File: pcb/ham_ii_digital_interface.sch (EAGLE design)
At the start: 21 parts, among them IC1 LM358N, T1 Left Driver, T2 Brake Driver, T3 Right Driver

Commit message: Changed value of C1 and changed C1 to an electrolytic capacitor.
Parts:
- C1: value 220p -> 1u; device resistor:C-US050-025X075 -> resistor:CPOL-USE2-5
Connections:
- net GND: now also C1.-; no longer C1.2
- net N$1: now also C1.+; no longer C1.1
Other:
- moved on the sheet: JP1, JP2
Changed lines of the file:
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@@
 <part name="D3" library="diode" deviceset="1N4148" device="DO35-7"/>
 <part name="JP2" library="pinhead" deviceset="PINHD-1X6" device="" value="Test"/>
-<part name="C1" library="resistor" deviceset="C-US" device="050-025X075" value="220p"/>
+<part name="C1" library="resistor" deviceset="CPOL-US" device="E2-5" value="1u"/>
 </parts>
 <sheets>
@@
 </plain>
 <instances>
-<instance part="JP1" gate="G$1" x="15.24" y="7.62"/>
-<instance part="JP2" gate="A" x="15.24" y="-12.7"/>
+<instance part="JP1" gate="G$1" x="17.78" y="7.62"/>
+<instance part="JP2" gate="A" x="17.78" y="-12.7"/>
 </instances>
 <busses>
@@
 <net name="LEFT_CONTROL_SIGNAL" class="0">
 <segment>
-<wire x1="12.7" y1="-5.08" x2="-22.86" y2="-5.08" width="0.1524" layer="91"/>
+<wire x1="15.24" y1="-5.08" x2="-22.86" y2="-5.08" width="0.1524" layer="91"/>
 <label x="-20.32" y="-5.08" size="1.778" layer="95"/>
 <pinref part="JP2" gate="A" pin="1"/>
@@
 <net name="BRAKE_CONTROL_SIGNAL" class="0">
 <segment>
-<wire x1="12.7" y1="-7.62" x2="-22.86" y2="-7.62" width="0.1524" layer="91"/>
+<wire x1="15.24" y1="-7.62" x2="-22.86" y2="-7.62" width="0.1524" layer="91"/>
 <label x="-20.32" y="-7.62" size="1.778" layer="95"/>
 <pinref part="JP2" gate="A" pin="2"/>
@@
 <net name="RIGHT_CONTROL_SIGNAL" class="0">
 <segment>
-<wire x1="12.7" y1="-10.16" x2="-22.86" y2="-10.16" width="0.1524" layer="91"/>
+<wire x1="15.24" y1="-10.16" x2="-22.86" y2="-10.16" width="0.1524" layer="91"/>
 <label x="-20.32" y="-10.16" size="1.778" layer="95"/>
 <pinref part="JP2" gate="A" pin="3"/>
@@
 <segment>
 <pinref part="JP1" gate="G$1" pin="2"/>
-<wire x1="12.7" y1="7.62" x2="-22.86" y2="7.62" width="0.1524" layer="91"/>
+<wire x1="15.24" y1="7.62" x2="-22.86" y2="7.62" width="0.1524" layer="91"/>
 <label x="-20.32" y="7.62" size="1.778" layer="95"/>
 </segment>
 <segment>
 <pinref part="JP2" gate="A" pin="6"/>
-<wire x1="12.7" y1="-17.78" x2="-22.86" y2="-17.78" width="0.1524" layer="91"/>
+<wire x1="15.24" y1="-17.78" x2="-22.86" y2="-17.78" width="0.1524" layer="91"/>
 <label x="-20.32" y="-17.78" size="1.778" layer="95"/>
 </segment>
@@
 <net name="ROTOR_POSITION_SIGNAL" class="0">
 <segment>
-<wire x1="12.7" y1="-12.7" x2="-22.86" y2="-12.7" width="0.1524" layer="91"/>
+<wire x1="15.24" y1="-12.7" x2="-22.86" y2="-12.7" width="0.1524" layer="91"/>
 <label x="-20.32" y="-12.7" size="1.778" layer="95"/>
 <pinref part="JP2" gate="A" pin="4"/>
@@
 <segment>
 <pinref part="JP1" gate="G$1" pin="1"/>
-<wire x1="12.7" y1="10.16" x2="-22.86" y2="10.16" width="0.1524" layer="91"/>
+<wire x1="15.24" y1="10.16" x2="-22.86" y2="10.16" width="0.1524" layer="91"/>
 <label x="-20.32" y="10.16" size="1.778" layer="95"/>
 </segment>
@@
 <net name="5V" class="0">
 <segment>
-<wire x1="12.7" y1="-15.24" x2="-22.86" y2="-15.24" width="0.1524" layer="91"/>
+<wire x1="15.24" y1="-15.24" x2="-22.86" y2="-15.24" width="0.1524" layer="91"/>
 <label x="-20.32" y="-15.24" size="1.778" layer="95"/>
 <pinref part="JP2" gate="A" pin="5"/>
@@
 <wire x1="-20.32" y1="-7.62" x2="-20.32" y2="-10.16" width="0.1524" layer="91"/>
 <label x="-20.32" y="-10.16" size="1.778" layer="95"/>
-<pinref part="C1" gate="G$1" pin="2"/>
+<pinref part="C1" gate="G$1" pin="-"/>
 </segment>
 </net>
@@
 <pinref part="R1" gate="G$1" pin="S"/>
 <wire x1="-7.62" y1="2.54" x2="-20.32" y2="2.54" width="0.1524" layer="91"/>
-<pinref part="C1" gate="G$1" pin="1"/>
 <wire x1="-20.32" y1="2.54" x2="-22.86" y2="2.54" width="0.1524" layer="91"/>
 <wire x1="-20.32" y1="0" x2="-20.32" y2="2.54" width="0.1524" layer="91"/>
 <junction x="-20.32" y="2.54"/>
-</segment>
-</net>
+<pinref part="C1" gate="G$1" pin="+"/>
+</segment>
+</net>

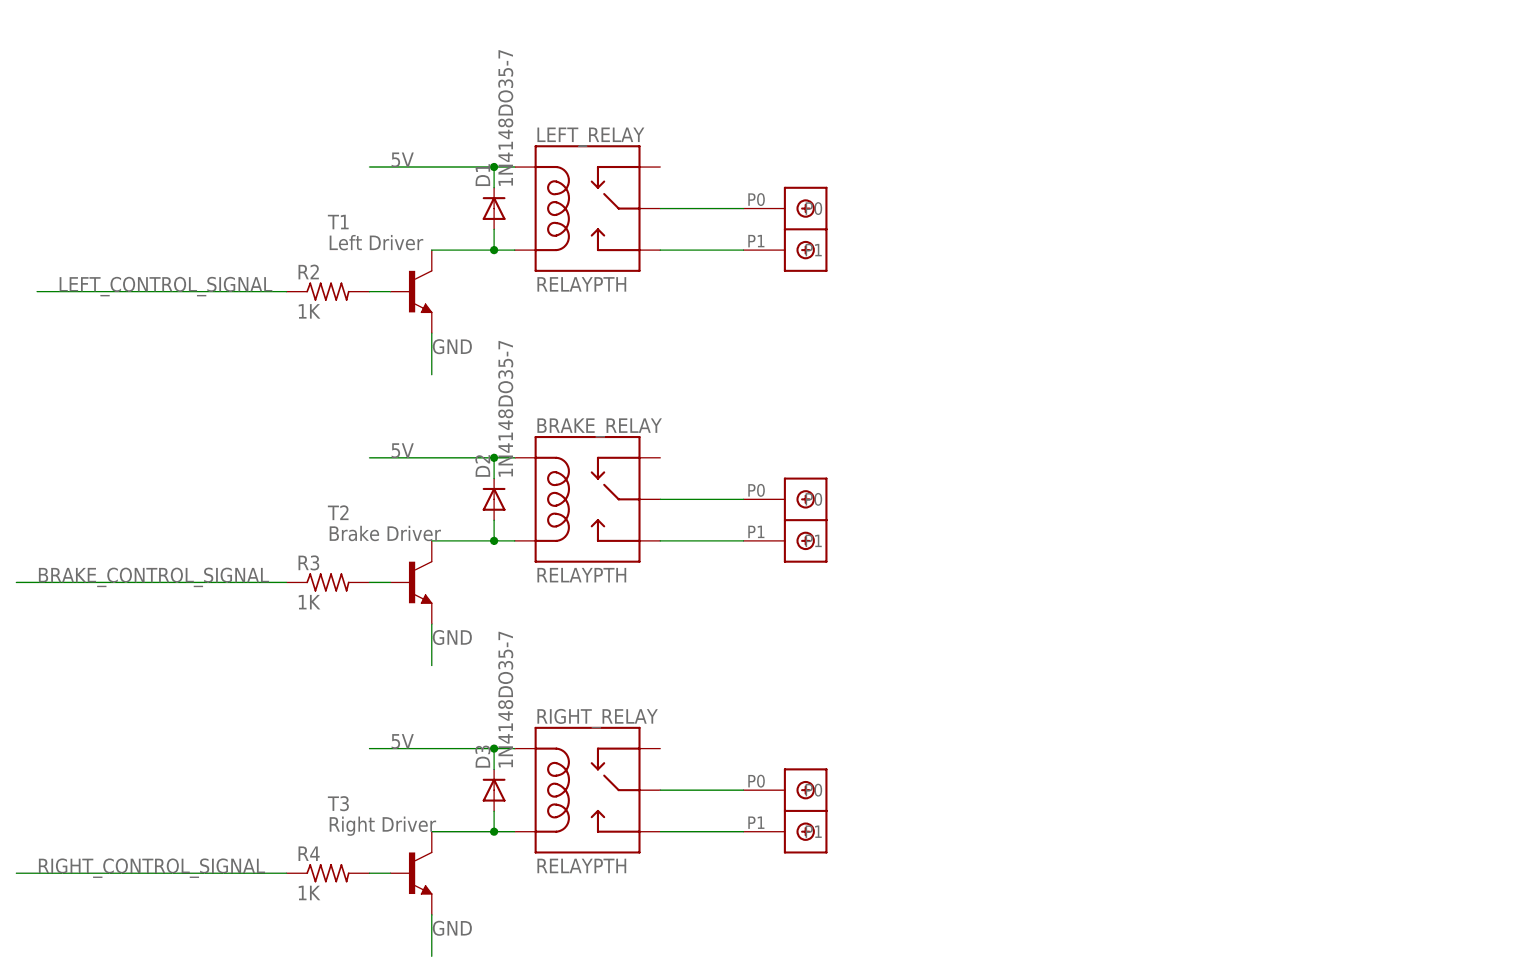
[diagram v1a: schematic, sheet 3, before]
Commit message: Fixed issue discovered after receiving print of PCB.  The NO and NC pins on the SRD-05VDC-SL-C schematic symbol are reveresed resulting in incorrect functionality.  Trace must be cut on NC pin and a jumper must be added for NO to correct previous revision of PCB.  Correction has been made to PCB, noted on schematic.
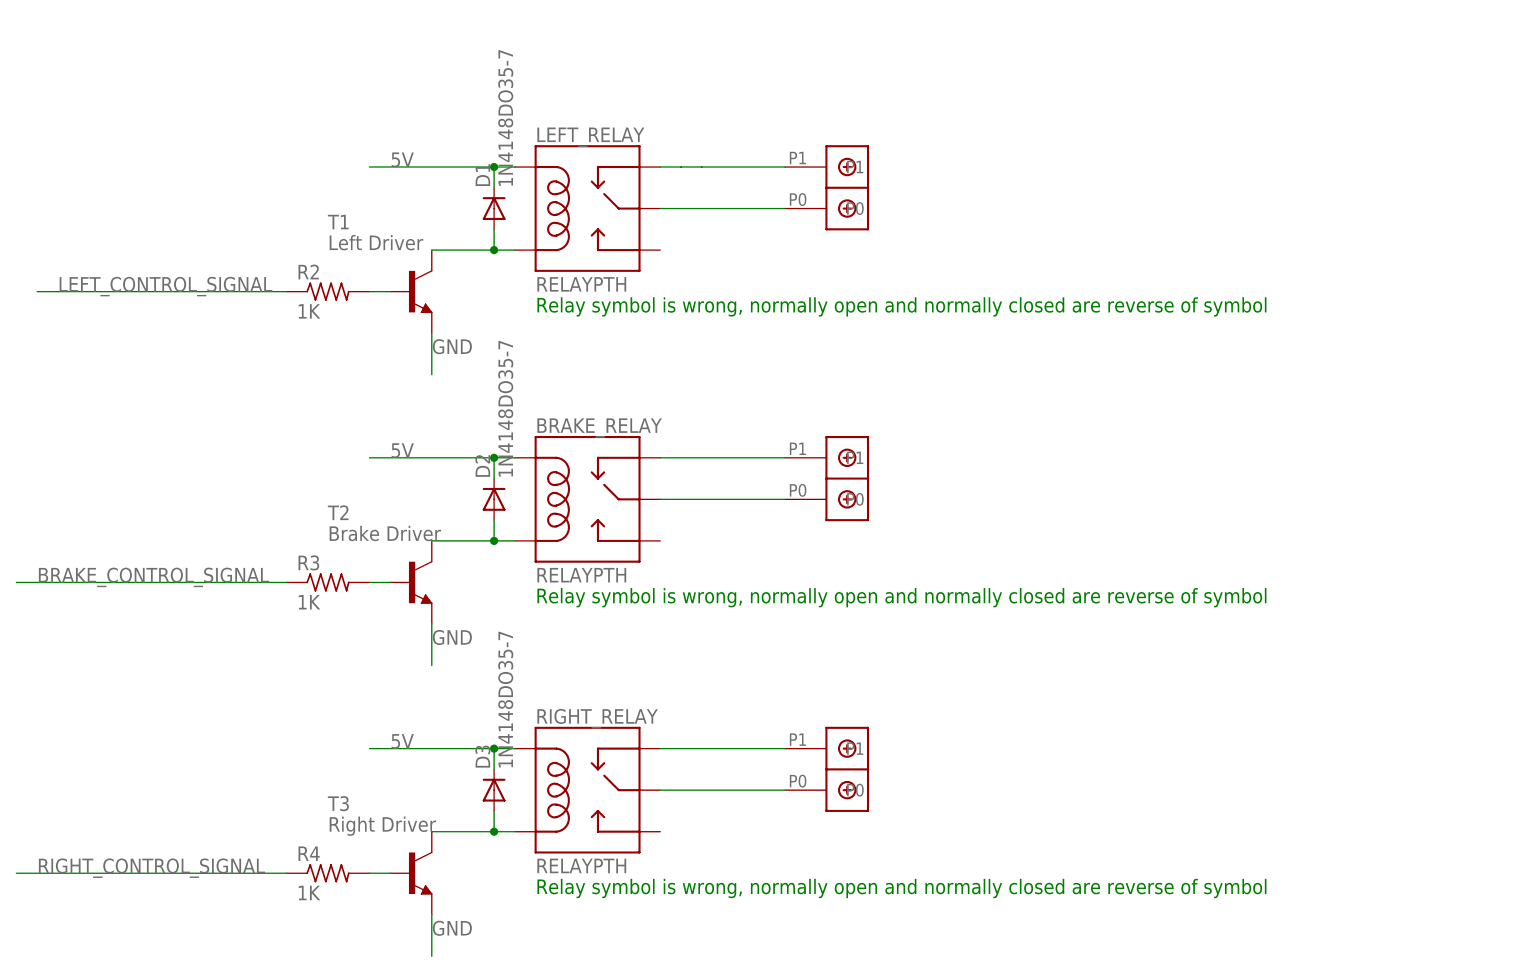
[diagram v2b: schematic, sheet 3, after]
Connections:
- net N$3: now also LEFT_RELAY.SWCLOSE; no longer LEFT_RELAY.SWOPEN
- net N$5: now also BRAKE_RELAY.SWCLOSE; no longer BRAKE_RELAY.SWOPEN
- net N$7: now also RIGHT_RELAY.SWCLOSE; no longer RIGHT_RELAY.SWOPEN
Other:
- note added: "Relay symbol is wrong, normally open and normally closed are reverse of symbol"
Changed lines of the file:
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@@
 <description>Relays</description>
 <plain>
+<text x="-7.62" y="-48.26" size="1.778" layer="91">Relay symbol is wrong, normally open and normally closed are reverse of symbol</text>
+<text x="-7.62" y="-12.7" size="1.778" layer="91">Relay symbol is wrong, normally open and normally closed are reverse of symbol</text>
+<text x="-7.62" y="22.86" size="1.778" layer="91">Relay symbol is wrong, normally open and normally closed are reverse of symbol</text>
 </plain>
 <instances>
@@
 <instance part="BRAKE_RELAY" gate="G$1" x="0" y="0"/>
 <instance part="RIGHT_RELAY" gate="G$1" x="0" y="-35.56"/>
-<instance part="U$5" gate="G$1" x="22.86" y="33.02"/>
-<instance part="U$6" gate="G$1" x="22.86" y="-2.54"/>
-<instance part="U$7" gate="G$1" x="22.86" y="-38.1"/>
+<instance part="U$5" gate="G$1" x="27.94" y="38.1" rot="MR180"/>
+<instance part="U$6" gate="G$1" x="27.94" y="2.54" rot="MR180"/>
+<instance part="U$7" gate="G$1" x="27.94" y="-33.02" rot="MR180"/>
 <instance part="T1" gate="G$1" x="-22.86" y="25.4"/>
 <instance part="T2" gate="G$1" x="-22.86" y="-10.16"/>
@@
 <pinref part="U$5" gate="G$1" pin="P0"/>
 <pinref part="LEFT_RELAY" gate="G$1" pin="SWCOMMON"/>
-<wire x1="17.78" y1="35.56" x2="7.62" y2="35.56" width="0.1524" layer="91"/>
-</segment>
-</net>
-<net name="N$3" class="0">
-<segment>
-<pinref part="LEFT_RELAY" gate="G$1" pin="SWOPEN"/>
-<pinref part="U$5" gate="G$1" pin="P1"/>
-<wire x1="7.62" y1="30.48" x2="17.78" y2="30.48" width="0.1524" layer="91"/>
+<wire x1="22.86" y1="35.56" x2="7.62" y2="35.56" width="0.1524" layer="91"/>
 </segment>
 </net>
@@
 <pinref part="BRAKE_RELAY" gate="G$1" pin="SWCOMMON"/>
 <pinref part="U$6" gate="G$1" pin="P0"/>
-<wire x1="7.62" y1="0" x2="17.78" y2="0" width="0.1524" layer="91"/>
-</segment>
-</net>
-<net name="N$5" class="0">
-<segment>
-<pinref part="BRAKE_RELAY" gate="G$1" pin="SWOPEN"/>
-<pinref part="U$6" gate="G$1" pin="P1"/>
-<wire x1="7.62" y1="-5.08" x2="17.78" y2="-5.08" width="0.1524" layer="91"/>
+<wire x1="7.62" y1="0" x2="22.86" y2="0" width="0.1524" layer="91"/>
 </segment>
 </net>
@@
 <pinref part="RIGHT_RELAY" gate="G$1" pin="SWCOMMON"/>
 <pinref part="U$7" gate="G$1" pin="P0"/>
-<wire x1="7.62" y1="-35.56" x2="17.78" y2="-35.56" width="0.1524" layer="91"/>
-</segment>
-</net>
-<net name="N$7" class="0">
-<segment>
-<pinref part="RIGHT_RELAY" gate="G$1" pin="SWOPEN"/>
-<pinref part="U$7" gate="G$1" pin="P1"/>
-<wire x1="7.62" y1="-40.64" x2="17.78" y2="-40.64" width="0.1524" layer="91"/>
+<wire x1="7.62" y1="-35.56" x2="22.86" y2="-35.56" width="0.1524" layer="91"/>
 </segment>
 </net>
@@
 </segment>
 </net>
+<net name="N$3" class="0">
+<segment>
+<pinref part="LEFT_RELAY" gate="G$1" pin="SWCLOSE"/>
+<wire x1="12.7" y1="40.64" x2="10.16" y2="40.64" width="0.1524" layer="91"/>
+<pinref part="U$5" gate="G$1" pin="P1"/>
+<wire x1="10.16" y1="40.64" x2="7.62" y2="40.64" width="0.1524" layer="91"/>
+<wire x1="22.86" y1="40.64" x2="12.7" y2="40.64" width="0.1524" layer="91"/>
+</segment>
+</net>
+<net name="N$5" class="0">
+<segment>
+<pinref part="BRAKE_RELAY" gate="G$1" pin="SWCLOSE"/>
+<pinref part="U$6" gate="G$1" pin="P1"/>
+<wire x1="22.86" y1="5.08" x2="7.62" y2="5.08" width="0.1524" layer="91"/>
+</segment>
+</net>
+<net name="N$7" class="0">
+<segment>
+<pinref part="RIGHT_RELAY" gate="G$1" pin="SWCLOSE"/>
+<pinref part="U$7" gate="G$1" pin="P1"/>
+<wire x1="22.86" y1="-30.48" x2="7.62" y2="-30.48" width="0.1524" layer="91"/>
+</segment>
+</net>
